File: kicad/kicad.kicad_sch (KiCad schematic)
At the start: 254 parts, among them J1 USB_A, J2 SWD, U1 AMS1117-3.3, Y1 16MGz, sw1 Esc, sw10 Z, sw100 N5, sw101 N6, sw102 N2, sw103 N1, sw104 N0, sw105 MPlay, sw106 MFwd, sw107 NSlash, sw108 NStar, sw109 N8, sw11 LCtrl, sw110 N9, sw111 NMinus, sw112 NPlus, sw113 NEnter, sw114 N3, sw115 NPeriod, sw12 LSys, sw13 F2, sw14 F3, sw15 2, sw16 3, sw17 W, sw18 E, sw19 S, sw2 F1, sw20 D, sw21 X, sw22 C, sw23 LAlt, sw24 THome, sw25 F4, sw26 F5, sw27 4, sw28 5, sw29 R, sw3 Tilda, sw30 T, sw31 F, sw32 G, sw33 V, sw34 B, sw35 LSpace, sw36 TLeft, sw37 F6, sw38 F7, sw39 6, sw4 1, sw40 7, sw41 Y, sw42 U, sw43 H, sw44 J, sw45 N, sw46 M, sw47 TUp, sw48 TDown, sw49 F8, sw5 Tab, sw50 F9, sw51 8, sw52 9, sw53 I, sw54 O, sw55 K, sw56 L, sw57 Comma, sw58 Period, sw59 RSpace, sw6 Q, sw60 TRight, sw61 F10, sw62 F11, sw63 0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

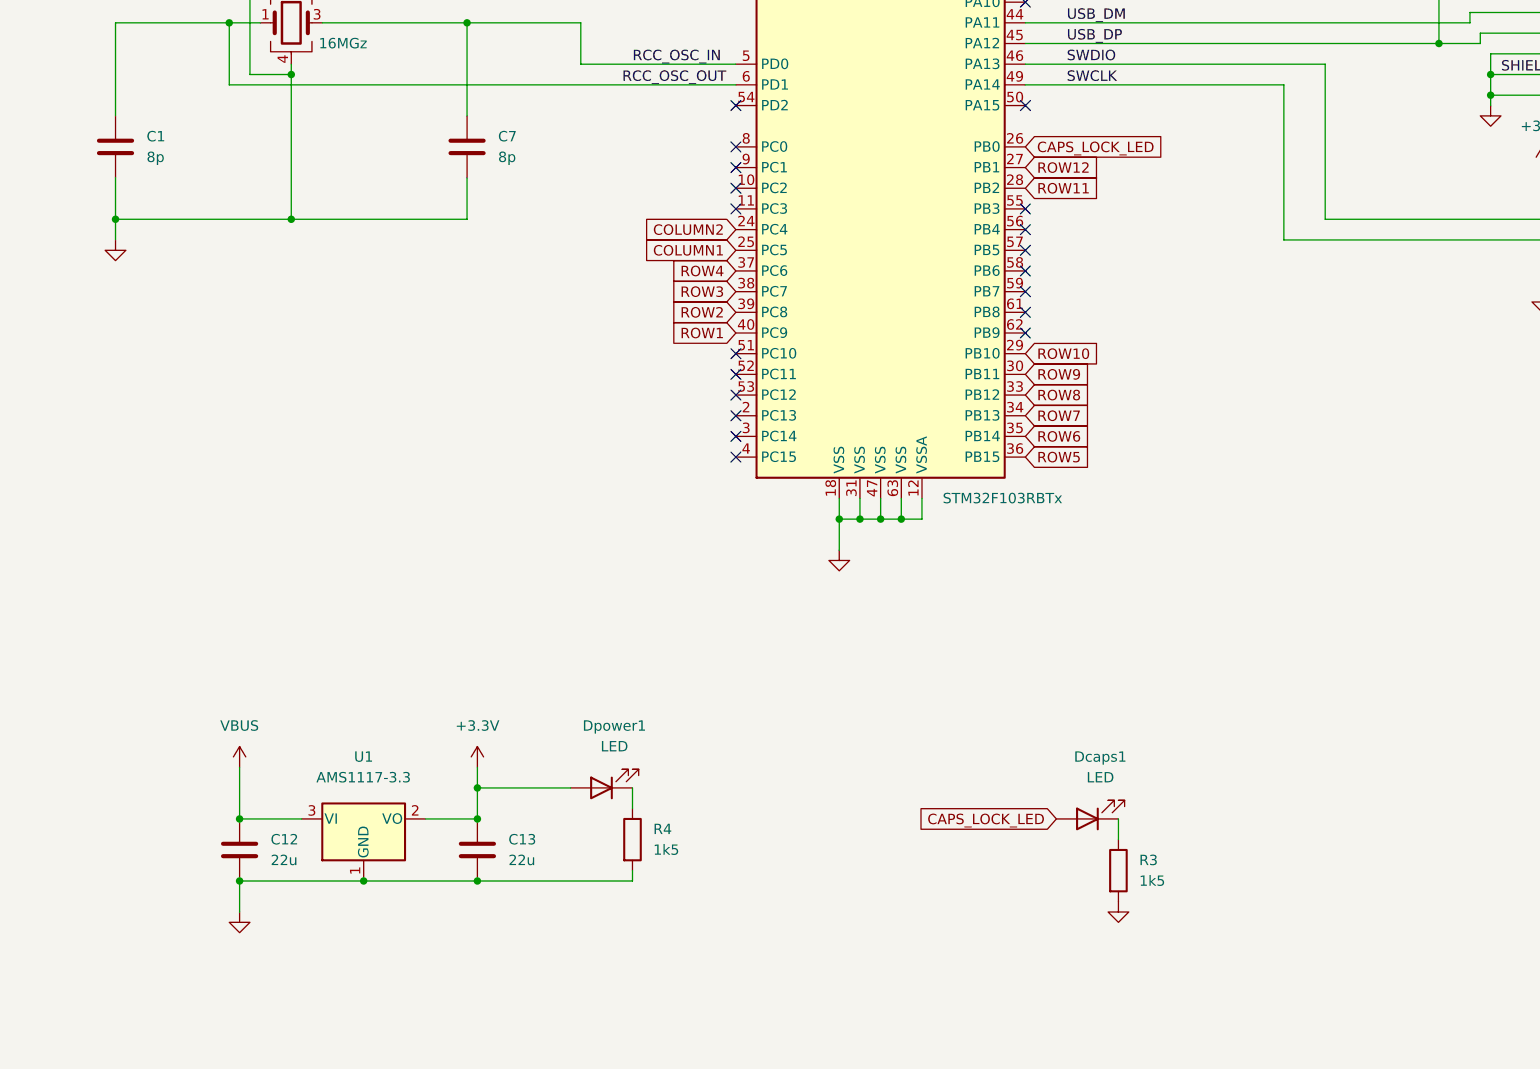
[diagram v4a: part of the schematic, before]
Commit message: All footprints selected, all parts sourced
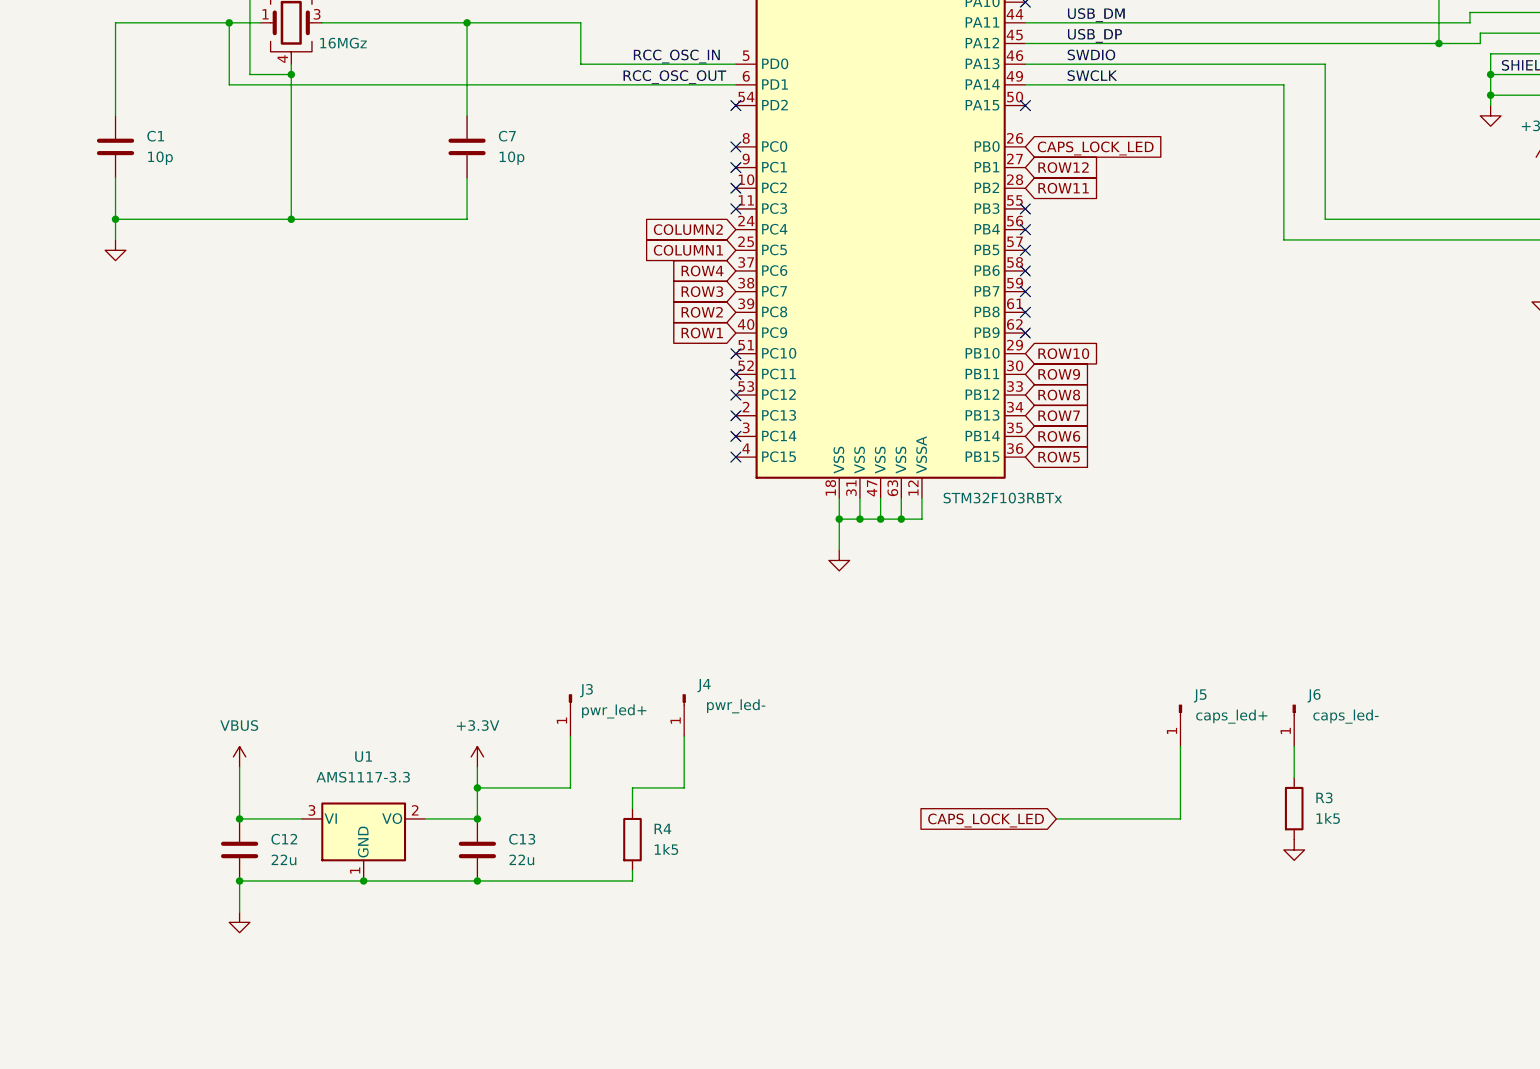
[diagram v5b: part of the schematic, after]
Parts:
- removed Dcaps1, Dpower1: LED, symbol Device:LED
- added J3: pwr_led+, Connector_PinHeader_2.54mm:PinHeader_1x01_P2.54mm_Vertical, symbol Connector:Conn_01x01_Male
- added J4: pwr_led-, Connector_PinHeader_2.54mm:PinHeader_1x01_P2.54mm_Vertical, symbol Connector:Conn_01x01_Male
- added J5: caps_led+, Connector_PinHeader_2.54mm:PinHeader_1x01_P2.54mm_Vertical, symbol Connector:Conn_01x01_Male
- added J6: caps_led-, Connector_PinHeader_2.54mm:PinHeader_1x01_P2.54mm_Vertical, symbol Connector:Conn_01x01_Male
- C1, C7: value 8p -> 10p; footprint (none) -> Capacitor_SMD:C_0603_1608Metric
- C10, C11, C3, C4, C5, C6, C8, C9: footprint (none) -> Capacitor_SMD:C_0402_1005Metric
- C12, C13: footprint (none) -> Capacitor_SMD:C_0805_2012Metric
- C2: footprint (none) -> Capacitor_SMD:C_0603_1608Metric
- J1: footprint (none) -> Connector_PinHeader_2.54mm:PinHeader_1x05_P2.54mm_Horizontal
- J2: footprint (none) -> Connector_PinHeader_2.54mm:PinHeader_1x04_P2.54mm_Vertical
- R1: footprint (none) -> Resistor_SMD:R_0402_1005Metric
- R2, R3, R4: footprint (none) -> Resistor_SMD:R_0603_1608Metric
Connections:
- net +3.3V: now also J3.1 (Pin_1)
- net CAPS_LOCK_LED: now also J5.1 (Pin_1)
- net at R4.1: now also J4.1 (Pin_1)
- net at R3.1: now also J6.1 (Pin_1)
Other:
- moved on the sheet: R3

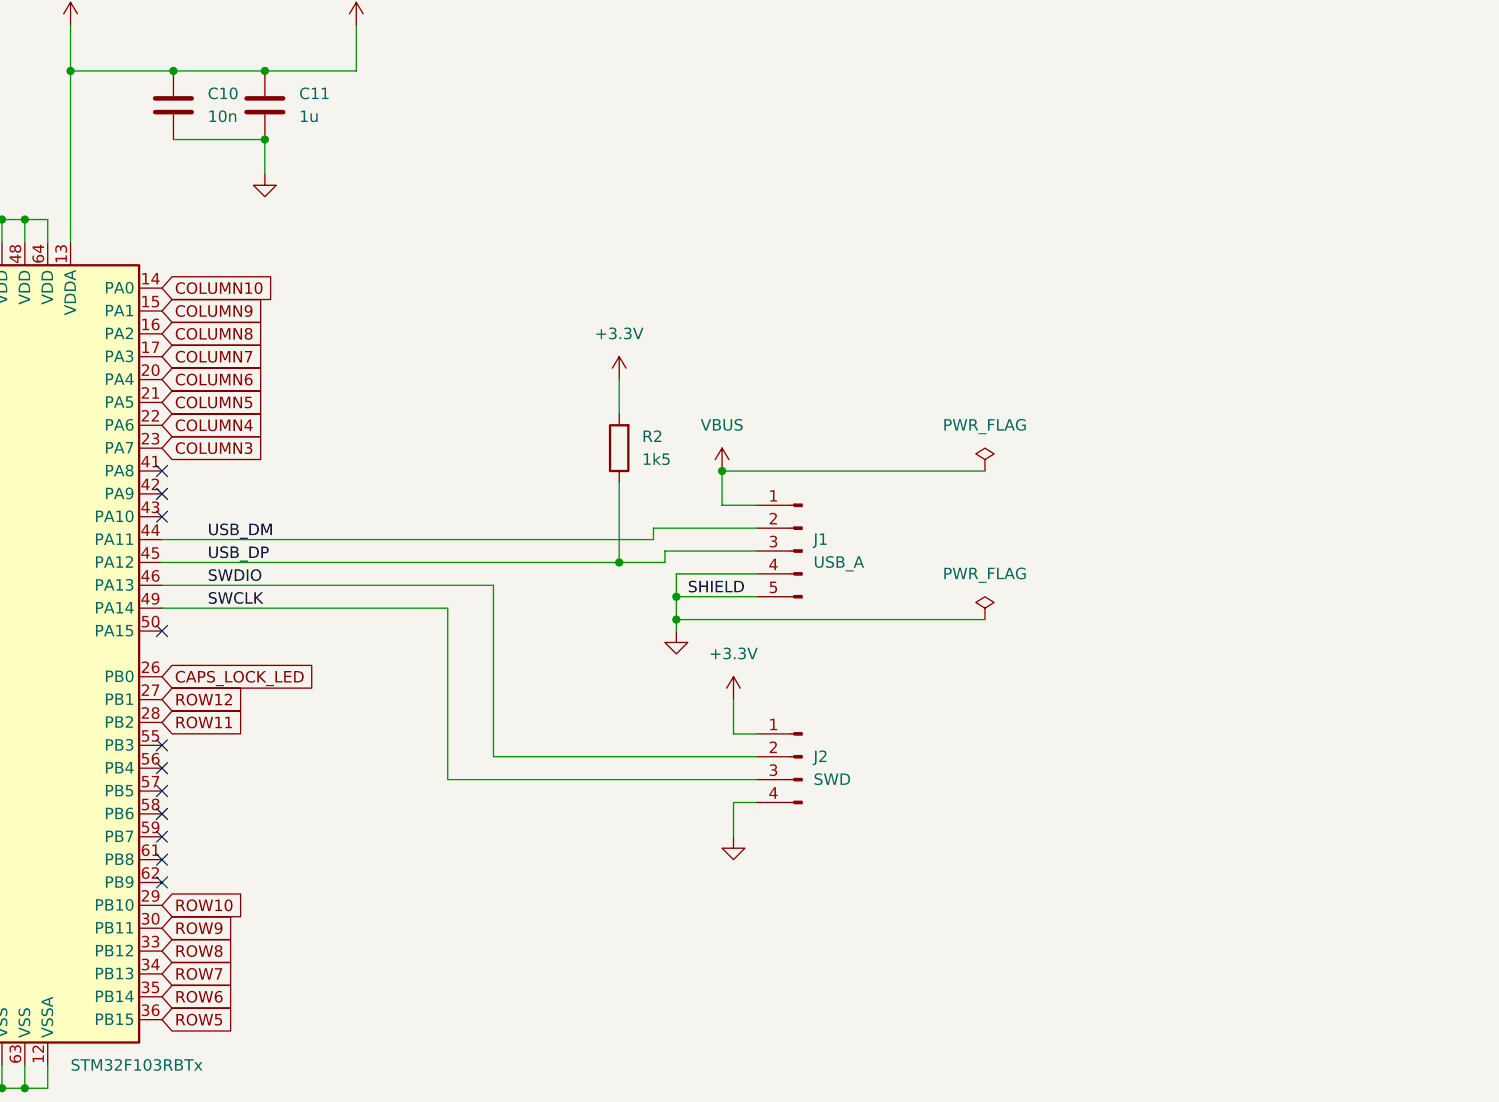
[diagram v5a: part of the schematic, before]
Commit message: component rough layout
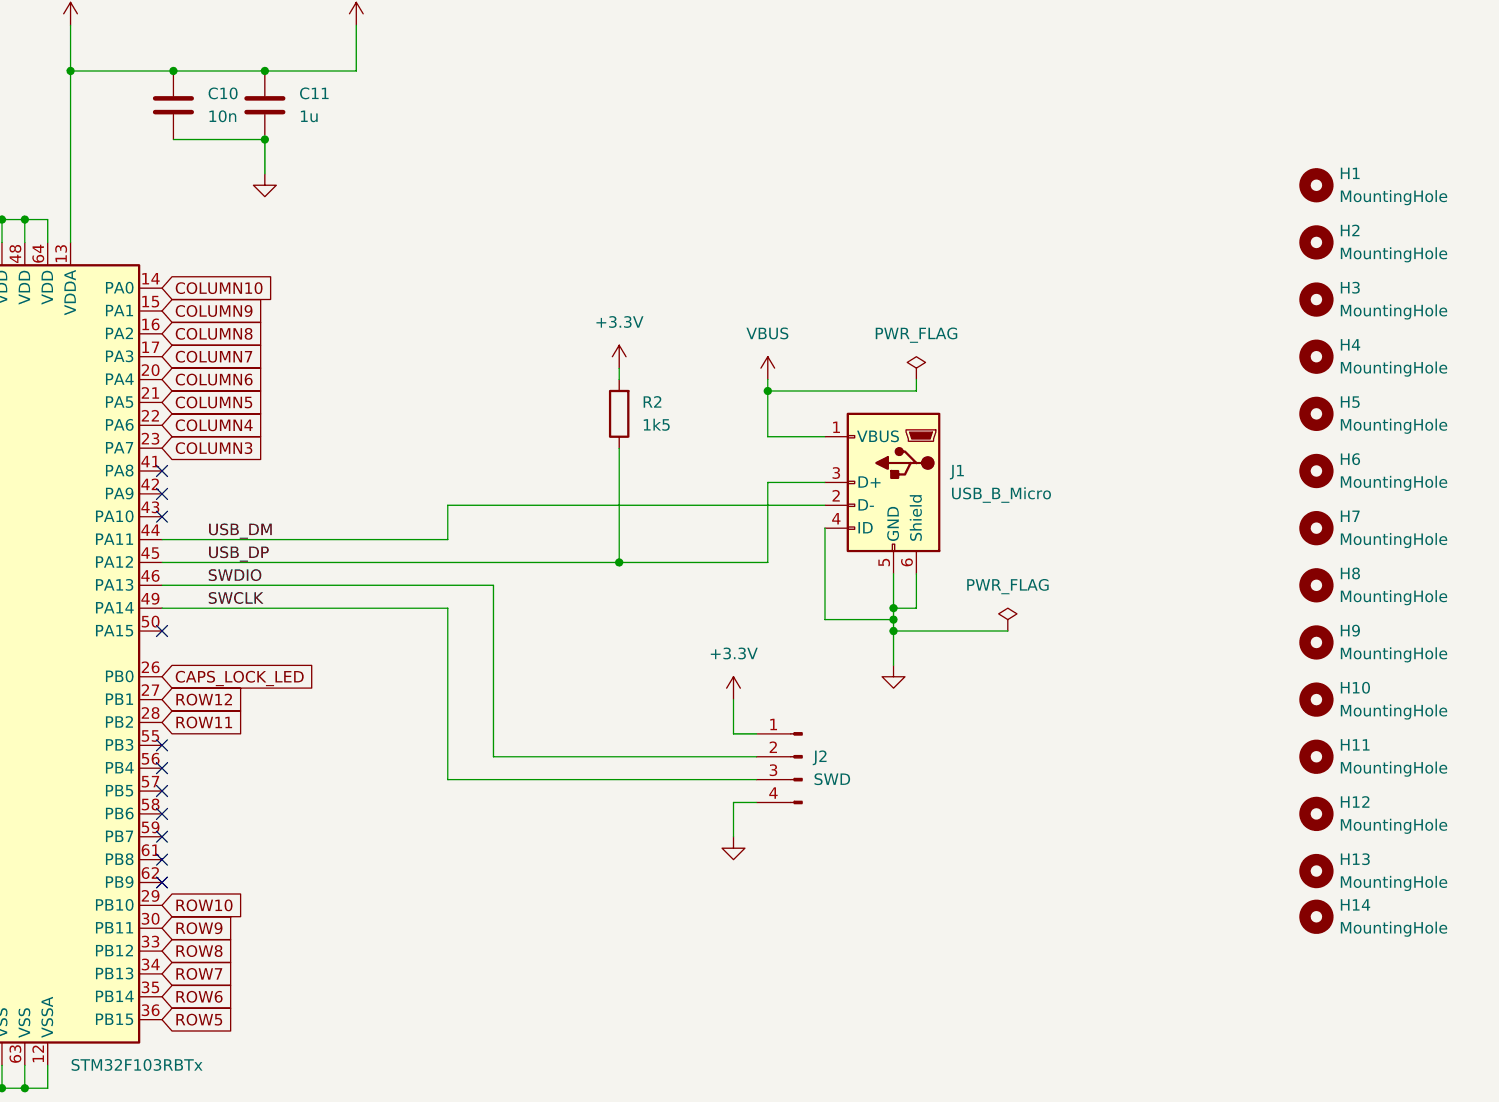
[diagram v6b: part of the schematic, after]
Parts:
- removed J1: USB_A, Connector_PinHeader_2.54mm:PinHeader_1x05_P2.54mm_Horizontal, symbol Connector:Conn_01x05_Male
- added H1, H10, H11, H12, H13, H14, H2, H3, H4, H5, H6, H7, H8, H9: MountingHole, MountingHole:MountingHole_2.2mm_M2, symbol Mechanical:MountingHole
- added J1: USB_B_Micro, Connector_USB:USB_Micro-B_Wuerth_629105150521, symbol Connector:USB_B_Micro
- C1, C7: footprint Capacitor_SMD:C_0603_1608Metric -> Capacitor_SMD:C_0402_1005Metric
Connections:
- net GND: now also J1.4 (ID), J1.5 (GND), J1.6 (Shield)
- net USB_DM: now also J1.2 (D-)
- net USB_DP: now also J1.3 (D+)
- net VBUS: now also J1.1 (VBUS)
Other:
- moved on the sheet: R2

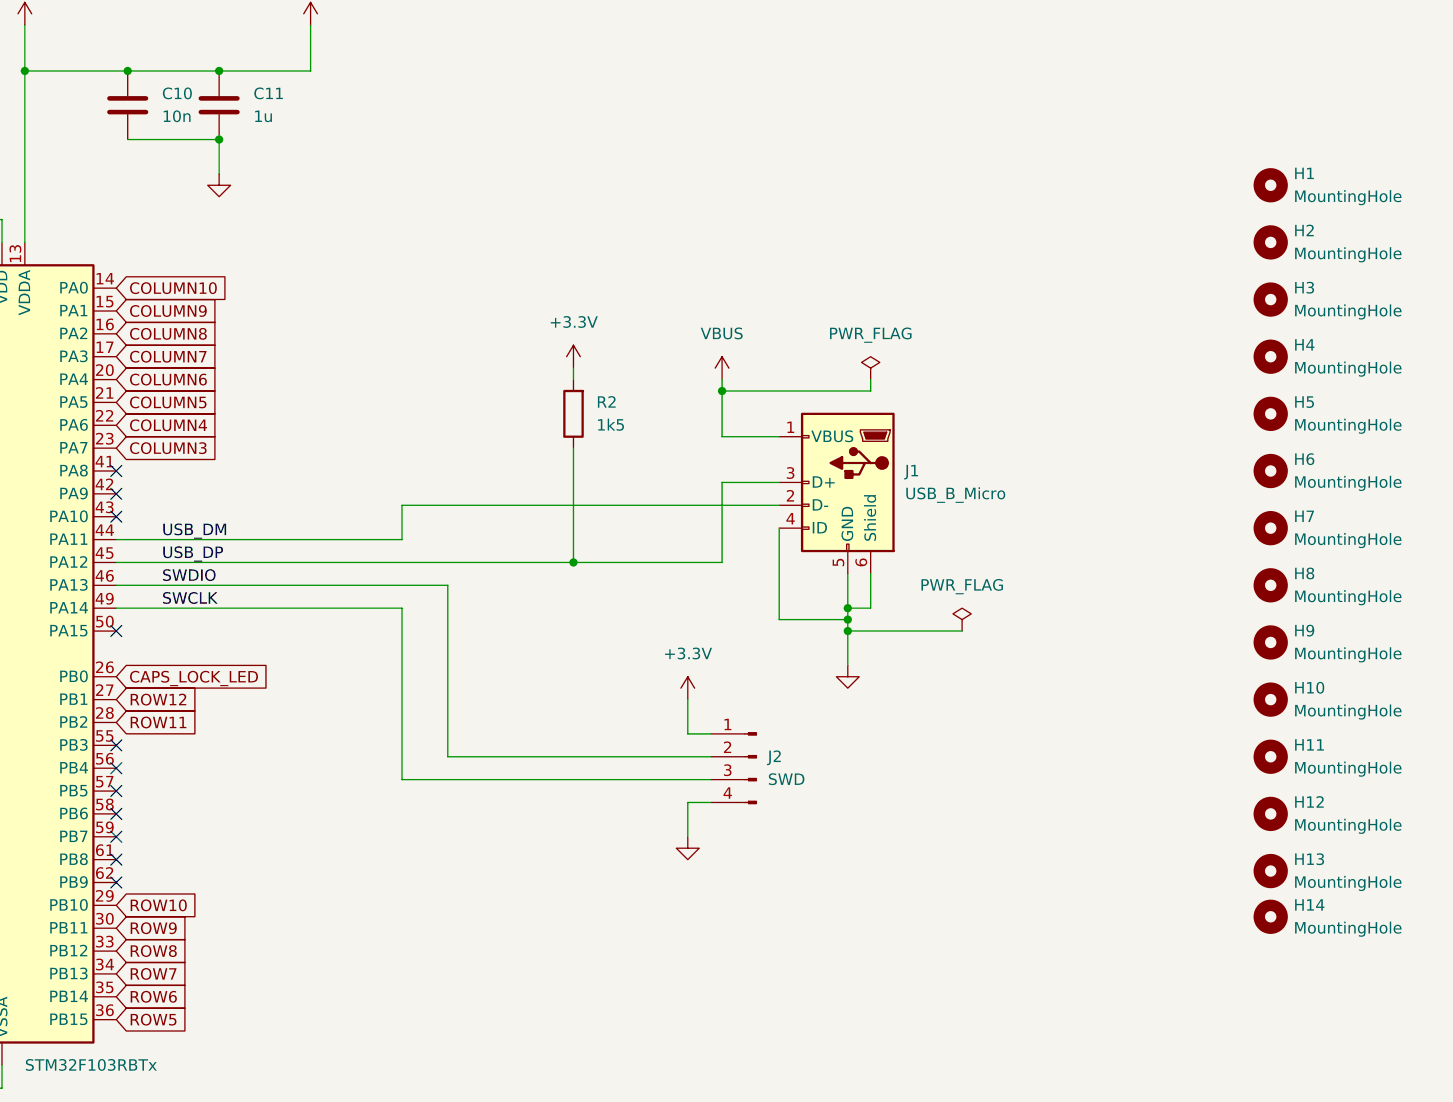
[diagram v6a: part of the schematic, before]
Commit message: getting close to pcb first draft
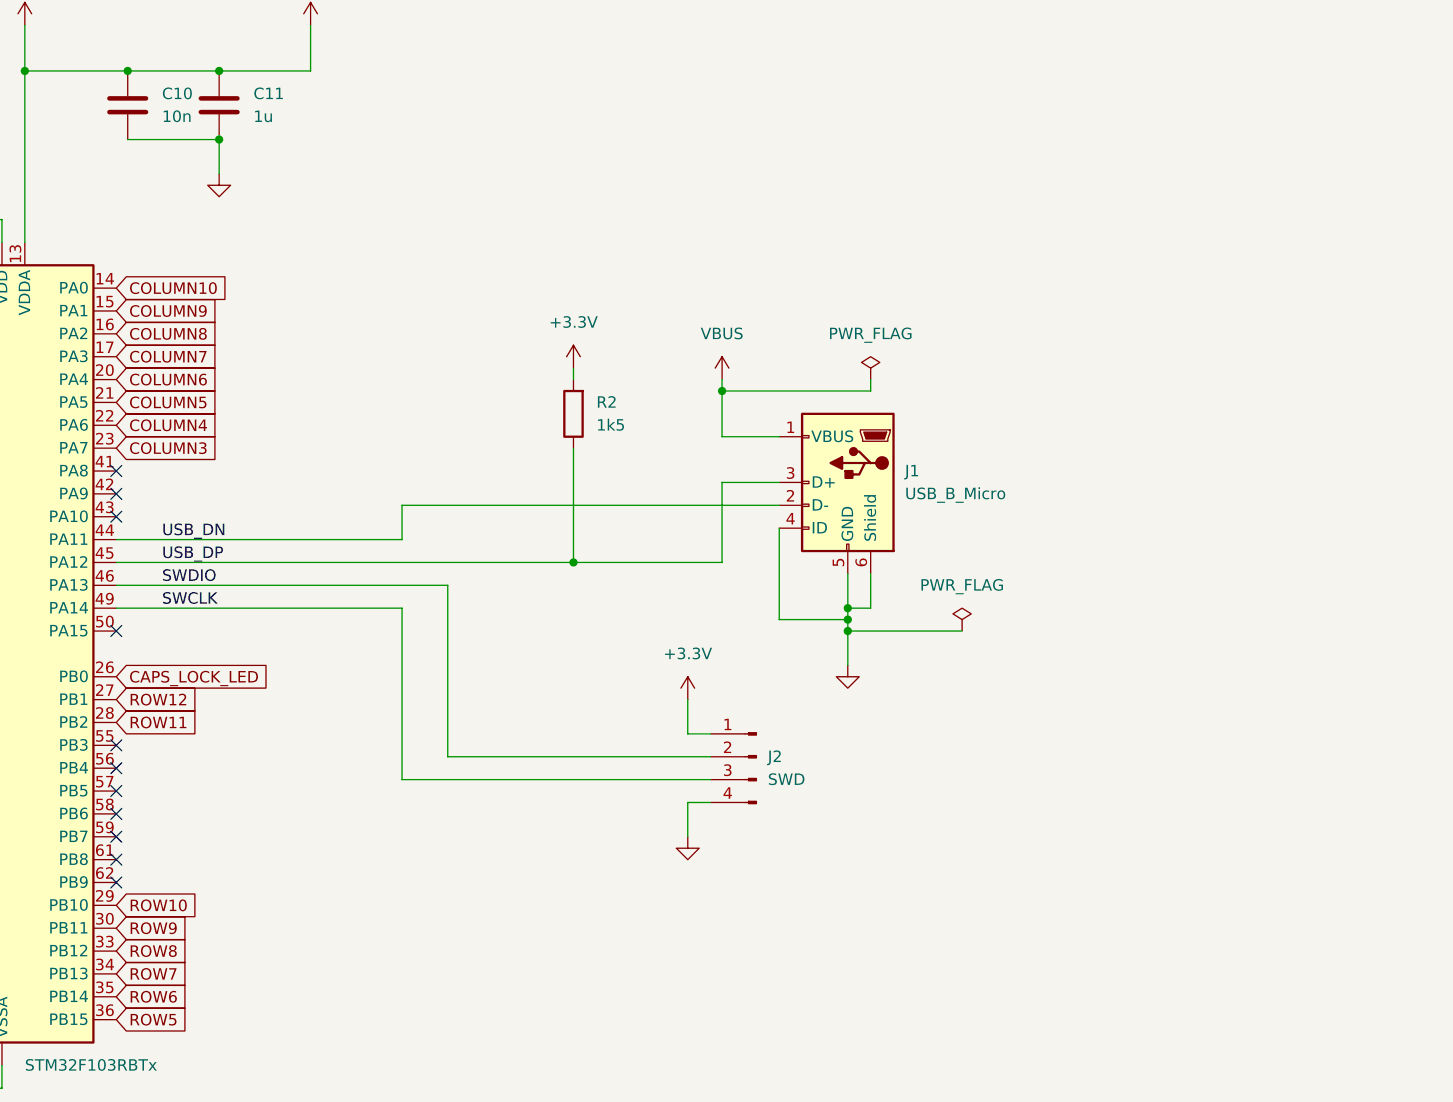
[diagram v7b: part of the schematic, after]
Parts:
- removed H1, H10, H11, H12, H13, H14, H2, H3, H4, H5, H6, H7, H8, H9: MountingHole, MountingHole:MountingHole_2.2mm_M2, symbol Mechanical:MountingHole
- R2: footprint Resistor_SMD:R_0603_1608Metric -> Resistor_SMD:R_0402_1005Metric
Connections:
- net USB_DM renamed USB_DN
